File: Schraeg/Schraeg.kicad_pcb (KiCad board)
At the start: 2 copper layers, 84.5 x 128.5 mm, 116 parts, among them U1 TL074, U2 TL074, U3 V2164, U4 TL074, U5 TL074

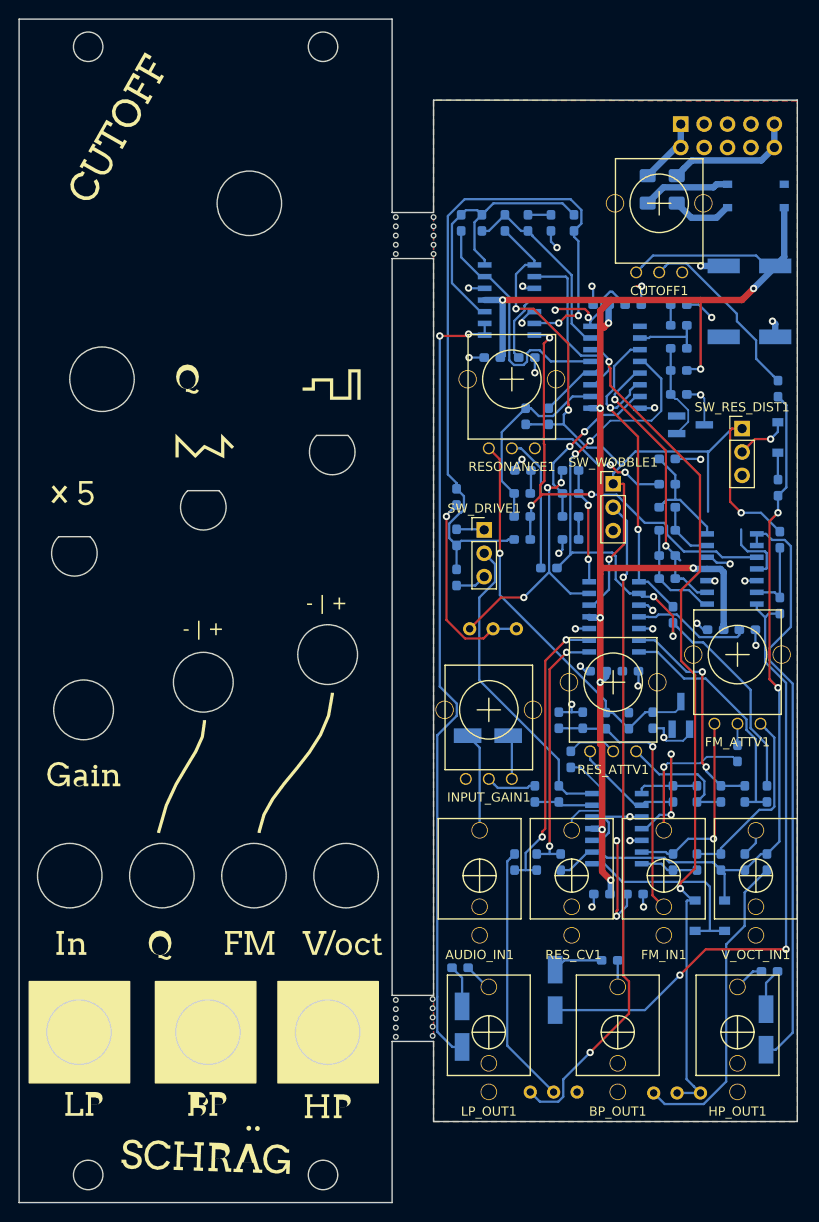
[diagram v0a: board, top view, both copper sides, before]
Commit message: Finished v0.2
* Flipped switches
* Enlarged switch holes
* Enlarged and enovaled pot support holes
* Reduced jack socket hole sizes
* Improved component and component reference locations

Archived v0.1 (previously know as the 2019 edition) and
re-exported schematics, gerbers, interactive BOM etc for
the 2021 Edition (v0.2).
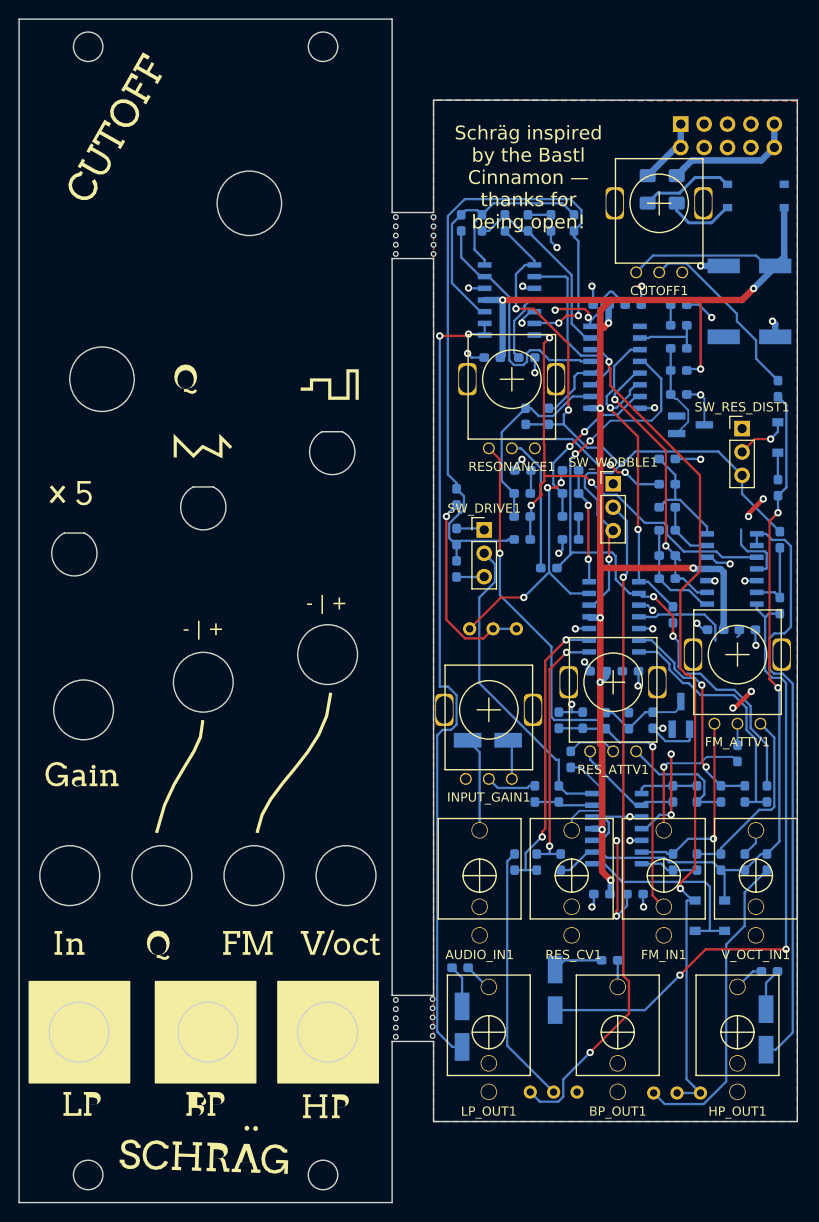
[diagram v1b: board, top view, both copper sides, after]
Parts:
- moved R22 4.45 mm to (47.5, 56.2), turned to 90 degrees
- moved R21 3.43 mm to (47.5, 59.7), turned to 270 degrees
- moved C2 0.50 mm to (50.9, 78.3)
- moved svg2mod 0.20 mm to (20.6, 64.5)
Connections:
- SW_DRIVE1 pad 1: Net-(R21-Pad2) -> Net-(R22-Pad2)
- SW_DRIVE1 pad 3: Net-(R22-Pad2) -> Net-(R21-Pad2)
- SW_RES_DIST1 pad 1: /Filter Core/RES_MOD -> (no net)
- SW_RES_DIST1 pad 3: (no net) -> /Filter Core/RES_MOD
- SW_WOBBLE1 pad 1: /Filter Core/RES_MOD -> (no net)
- SW_WOBBLE1 pad 3: (no net) -> /Filter Core/RES_MOD
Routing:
- net /Filter Core/RES_MOD: track 95.3 -> 83.3 mm, vias 4 -> 3
- net 5V_REF: track 44.7 -> 49.1 mm
- net +12V: track 61.8 -> 65.9 mm, vias 6 -> 10
- net Net-(C11-Pad2): track 23.8 -> 25.3 mm
- net /Filter Core/HP_OUT: track 64.0 -> 65.2 mm
- net GND: track 76.1 -> 77.3 mm
- net Net-(R13-Pad1): track 26.5 -> 27.6 mm
- net /Filter Core/LP_OUT: track 86.9 -> 87.9 mm
- net Net-(D5-Pad1): track 6.64 -> 7.57 mm
- net /Filter Core/AUDIO_IN: track 79.5 -> 78.7 mm
- net Net-(D5-Pad2): track 9.52 -> 10.1 mm
- net Net-(R28-Pad1): track 51.5 -> 52.1 mm
- net /Filter Core/BP_OUT: track 68.4 -> 68.9 mm
- net Net-(R11-Pad1): track 24.1 -> 23.6 mm
- net Net-(AUDIO_IN1-Pad3): track 10.8 -> 10.3 mm
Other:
- outline, holes or cut-outs redrawn
- board text added: "Schräg inspired by the Bastl Cinnamon — thanks for being open!"
- board text added: "Schräg v0.2 Barnaby Walters waterpigs.co.uk cc-by-sa 2021"
- board text removed: "Barnaby Walters waterpigs.co.uk cc-by-sa 2019"

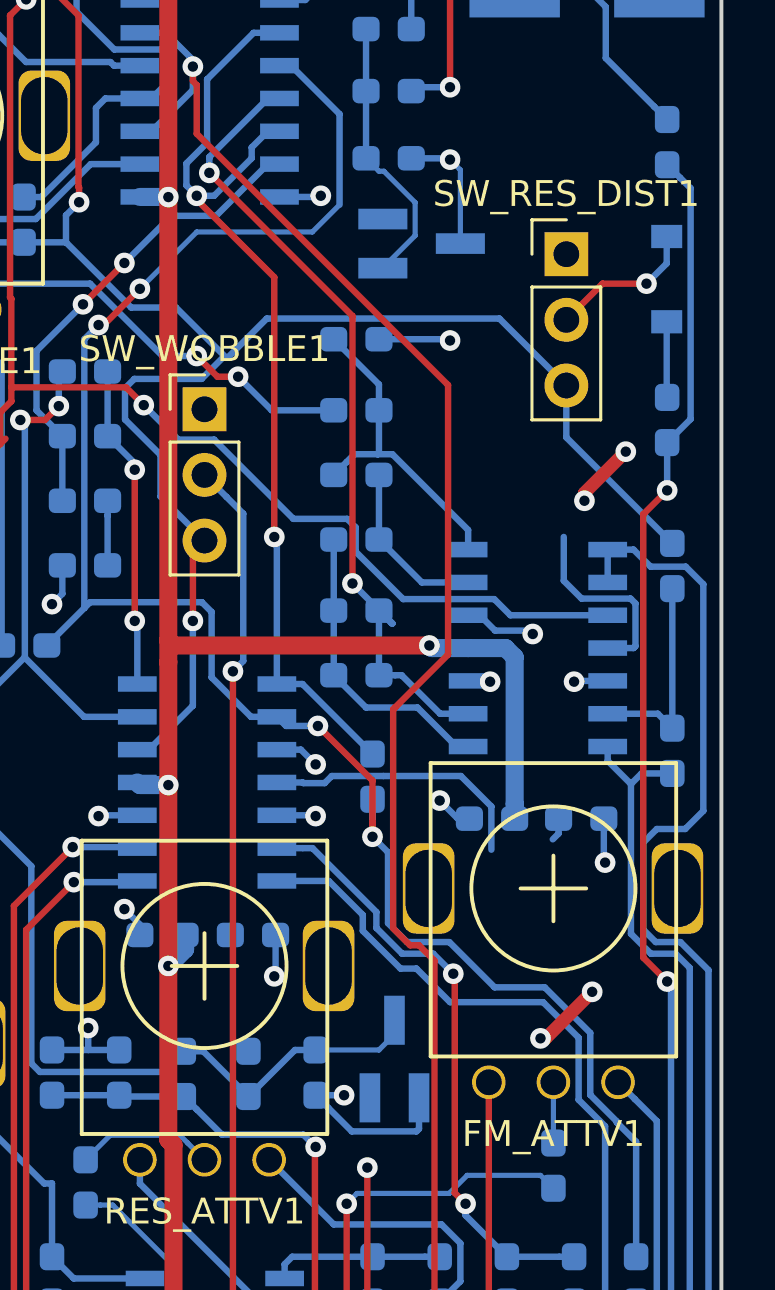
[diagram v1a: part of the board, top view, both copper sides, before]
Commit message: Fixed LM4040 symbols and PCB layout. Fixes #2
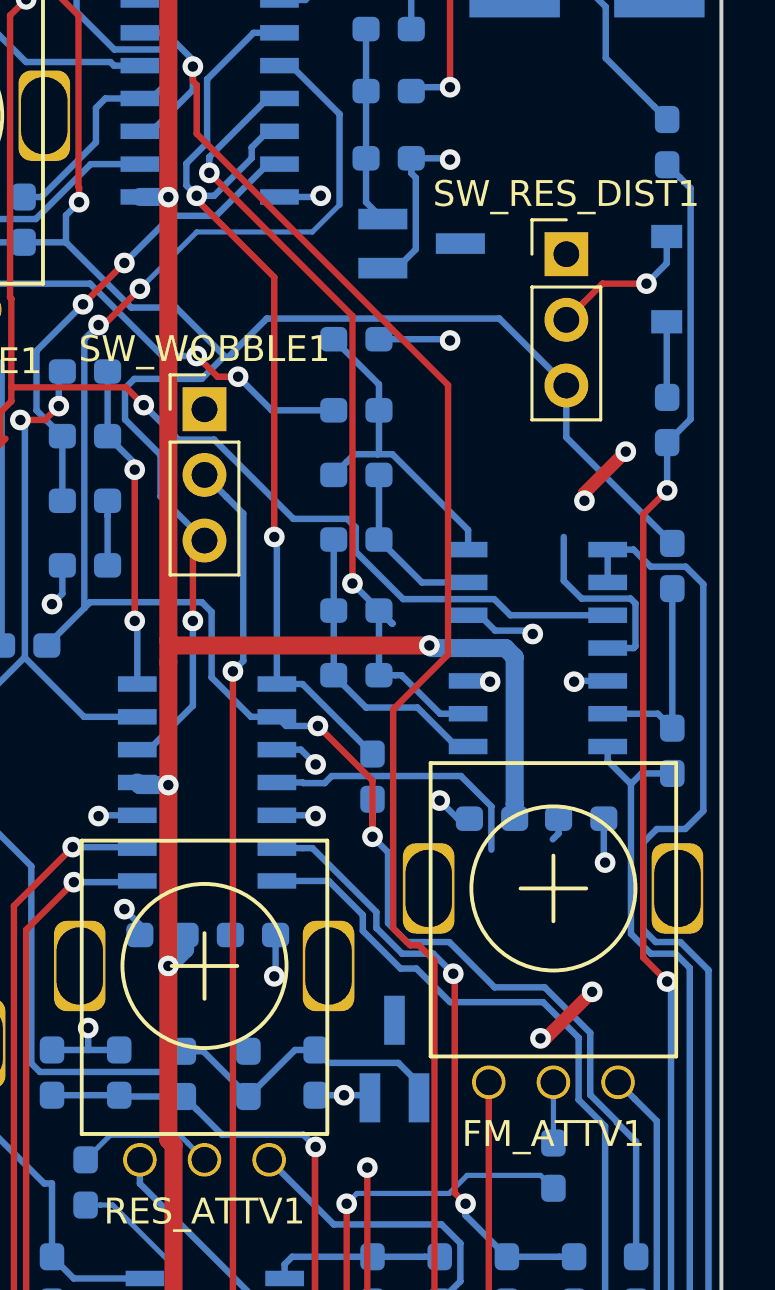
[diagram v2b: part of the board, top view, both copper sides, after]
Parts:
- D4, D6: value LM4040DCK-5 -> LM4040DBZ-5
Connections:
- D4 pad 1: GND -> 5V_REF
- D4 pad 2: (no net) -> GND
- D4 pad 3: 5V_REF -> (no net)
- D6 pad 1: -5V_REF -> GND
- D6 pad 2: (no net) -> -5V_REF
- D6 pad 3: GND -> (no net)
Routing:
- net -5V_REF: track 10.7 -> 7.62 mm
- net GND: track 77.3 -> 74.3 mm
- net 5V_REF: track 49.1 -> 50.4 mm
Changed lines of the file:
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@@
     (thickness 1.6)
     (drawings 233)
-    (tracks 934)
+    (tracks 932)
     (zones 0)
     (modules 116)
@@
       (effects (font (size 1 1) (thickness 0.15)) (justify mirror))
     )
-    (fp_text value LM4040DCK-5 (at 0 -2.5 90) (layer B.Fab)
+    (fp_text value LM4040DBZ-5 (at 0 -2.5 90) (layer B.Fab)
       (effects (font (size 1 1) (thickness 0.15)) (justify mirror))
     )
@@
       (effects (font (size 0.5 0.5) (thickness 0.075)) (justify mirror))
     )
-    (pad 3 smd rect (at 1.5 0 90) (size 1.9 0.8) (layers B.Cu B.Paste B.Mask)
-      (net 24 5V_REF))
-    (pad 2 smd rect (at -1.5 -0.95 90) (size 1.9 0.8) (layers B.Cu B.Paste B.Mask))
-    (pad 1 smd rect (at -1.5 0.95 90) (size 1.9 0.8) (layers B.Cu B.Paste B.Mask)
+    (pad 3 smd rect (at 1.5 0 90) (size 1.9 0.8) (layers B.Cu B.Paste B.Mask))
+    (pad 2 smd rect (at -1.5 -0.95 90) (size 1.9 0.8) (layers B.Cu B.Paste B.Mask)
       (net 1 GND))
+    (pad 1 smd rect (at -1.5 0.95 90) (size 1.9 0.8) (layers B.Cu B.Paste B.Mask)
+      (net 24 5V_REF))
     (model ${KISYS3DMOD}/Package_TO_SOT_SMD.3dshapes/SOT-23.wrl
       (at (xyz 0 0 0))
@@
       (effects (font (size 1 1) (thickness 0.15)) (justify mirror))
     )
-    (fp_text value LM4040DCK-5 (at 0 -2.5) (layer B.Fab)
+    (fp_text value LM4040DBZ-5 (at 0 -2.5) (layer B.Fab)
       (effects (font (size 1 1) (thickness 0.15)) (justify mirror))
     )
@@
     (fp_line (start 0.76 -1.58) (end -0.7 -1.58) (layer B.SilkS) (width 0.12))
     (pad 1 smd rect (at -1.5 0.95) (size 1.9 0.8) (layers B.Cu B.Paste B.Mask)
-      (net 28 -5V_REF))
-    (pad 2 smd rect (at -1.5 -0.95) (size 1.9 0.8) (layers B.Cu B.Paste B.Mask))
-    (pad 3 smd rect (at 1.5 0) (size 1.9 0.8) (layers B.Cu B.Paste B.Mask)
       (net 1 GND))
+    (pad 2 smd rect (at -1.5 -0.95) (size 1.9 0.8) (layers B.Cu B.Paste B.Mask)
+      (net 28 -5V_REF))
+    (pad 3 smd rect (at 1.5 0) (size 1.9 0.8) (layers B.Cu B.Paste B.Mask))
     (model ${KISYS3DMOD}/Package_TO_SOT_SMD.3dshapes/SOT-23.wrl
       (at (xyz 0 0 0))
@@
   (segment (start 67.4 42.245) (end 68.955 42.245) (width 0.25) (layer B.Cu) (net 1))
   (via (at 74 40.8) (size 0.8) (drill 0.4) (layers F.Cu B.Cu) (net 1))
-  (segment (start 73.95 40.75) (end 74 40.8) (width 0.25) (layer B.Cu) (net 1))
   (segment (start 72.5 40.75) (end 73.95 40.75) (width 0.25) (layer B.Cu) (net 1))
+  (segment (start 73.95 40.75) (end 74 40.8) (width 0.25) (layer B.Cu) (net 1))
   (via (at 74 47.8) (size 0.8) (drill 0.4) (layers F.Cu B.Cu) (net 1))
   (segment (start 73.95 47.75) (end 74 47.8) (width 0.25) (layer B.Cu) (net 1))
@@
   (segment (start 75.74499 59.02499) (end 77.06999 59.02499) (width 0.25) (layer B.Cu) (net 1))
   (segment (start 74.7 58.43) (end 75.15 58.43) (width 0.25) (layer B.Cu) (net 1))
-  (segment (start 74.399999 41.199999) (end 74 40.8) (width 0.2) (layer B.Cu) (net 1))
-  (segment (start 74.4 44.05) (end 74.399999 41.199999) (width 0.2) (layer B.Cu) (net 1))
   (segment (start 49.15 36.75) (end 48.7 36.3) (width 0.25) (layer B.Cu) (net 1))
   (via (at 48.7 36.3) (size 0.8) (drill 0.4) (layers F.Cu B.Cu) (net 1))
@@
   (segment (start 62 70.4) (end 61.4 69.8) (width 0.25) (layer B.Cu) (net 1))
   (segment (start 62 70.8) (end 62 70.4) (width 0.25) (layer B.Cu) (net 1))
-  (segment (start 69.299072 77.499072) (end 68.8 77) (width 0.25) (layer B.Cu) (net 1))
-  (segment (start 72.8 78.3) (end 72.7 78.4) (width 0.25) (layer B.Cu) (net 1))
-  (segment (start 70.2 78.4) (end 69.299072 77.499072) (width 0.25) (layer B.Cu) (net 1))
-  (segment (start 72.7 78.4) (end 70.2 78.4) (width 0.25) (layer B.Cu) (net 1))
-  (segment (start 72.8 77.1) (end 72.8 78.3) (width 0.25) (layer B.Cu) (net 1))
   (via (at 69.899998 77) (size 0.8) (drill 0.4) (layers F.Cu B.Cu) (net 1))
   (segment (start 68.8 77) (end 69.899998 77) (width 0.25) (layer B.Cu) (net 1))
@@
   (segment (start 64.45 75.3) (end 63.7 75.3) (width 0.25) (layer B.Cu) (net 24))
   (segment (start 66.2 77.05) (end 64.45 75.3) (width 0.25) (layer B.Cu) (net 24))
-  (segment (start 71.85 74.65) (end 71.85 74.1) (width 0.2) (layer B.Cu) (net 24))
-  (segment (start 71.25 75.25) (end 71.85 74.65) (width 0.2) (layer B.Cu) (net 24))
-  (segment (start 68.8 75.25) (end 71.25 75.25) (width 0.2) (layer B.Cu) (net 24))
   (segment (start 57.79999 68.138988) (end 57.79999 75.7705) (width 0.25) (layer B.Cu) (net 24))
   (segment (start 57.79999 75.7705) (end 58.12949 76.1) (width 0.25) (layer B.Cu) (net 24))
@@
   (segment (start 70.75 35.75) (end 70.75 38.15) (width 0.25) (layer B.Cu) (net 28))
   (segment (start 70.75 38.15) (end 70.75 40.75) (width 0.25) (layer B.Cu) (net 28))
-  (segment (start 71.249072 41.249072) (end 70.75 40.75) (width 0.2) (layer B.Cu) (net 28))
-  (segment (start 72.650001 42.459999) (end 71.439074 41.249072) (width 0.2) (layer B.Cu) (net 28))
-  (segment (start 71.439074 41.249072) (end 71.249072 41.249072) (width 0.2) (layer B.Cu) (net 28))
-  (segment (start 72.650001 43.740001) (end 72.650001 42.459999) (width 0.2) (layer B.Cu) (net 28))
-  (segment (start 71.390002 45) (end 72.650001 43.740001) (width 0.2) (layer B.Cu) (net 28))
-  (segment (start 71.4 45) (end 71.390002 45) (width 0.2) (layer B.Cu) (net 28))
+  (segment (start 71.4 45) (end 71.390002 45) (width 0.2) (layer B.Cu) (net 1))
+  (segment (start 70.8 77) (end 70.9 77.1) (width 0.25) (layer B.Cu) (net 1))
+  (segment (start 69.899998 77) (end 70.8 77) (width 0.25) (layer B.Cu) (net 1))
+  (segment (start 72.675001 44.274999) (end 71.95 45) (width 0.25) (layer B.Cu) (net 1))
+  (segment (start 72.675001 41.500001) (end 72.675001 44.274999) (width 0.25) (layer B.Cu) (net 1))
+  (segment (start 72.5 41.325) (end 72.675001 41.500001) (width 0.25) (layer B.Cu) (net 1))
+  (segment (start 71.95 45) (end 71.4 45) (width 0.25) (layer B.Cu) (net 1))
+  (segment (start 72.5 40.75) (end 72.5 41.325) (width 0.25) (layer B.Cu) (net 1))
+  (segment (start 72.8 76.55) (end 72.8 77.1) (width 0.25) (layer B.Cu) (net 24))
+  (segment (start 71.999072 75.749072) (end 72.8 76.55) (width 0.25) (layer B.Cu) (net 24))
+  (segment (start 69.299072 75.749072) (end 71.999072 75.749072) (width 0.25) (layer B.Cu) (net 24))
+  (segment (start 68.8 75.25) (end 69.299072 75.749072) (width 0.25) (layer B.Cu) (net 24))
+  (segment (start 70.75 42.45) (end 71.4 43.1) (width 0.25) (layer B.Cu) (net 28))
+  (segment (start 70.75 40.75) (end 70.75 42.45) (width 0.25) (layer B.Cu) (net 28))
   (segment (start 81.900928 38.750928) (end 82.4 39.25) (width 0.25) (layer B.Cu) (net 29))
   (segment (start 80.024999 34.889997) (end 80.024999 36.874999) (width 0.25) (layer B.Cu) (net 29))

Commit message: Updated board version reference
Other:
- board text added: "Schräg v0.2.1 Barnaby Walters waterpigs.co.uk cc-by-sa 2021"
- board text removed: "Schräg v0.2 Barnaby Walters waterpigs.co.uk cc-by-sa 2021"
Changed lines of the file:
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@@
   (gr_circle (center 20.5 110) (end 23.75 110) (layer Edge.Cuts) (width 0.15))
   (gr_circle (center 6.5 110) (end 9.75 110) (layer Edge.Cuts) (width 0.15))
-  (gr_text "Schräg v0.2\nBarnaby Walters\nwaterpigs.co.uk\ncc-by-sa 2021" (at 53.7 13.2) (layer B.SilkS)
+  (gr_text "Schräg v0.2.1\nBarnaby Walters\nwaterpigs.co.uk\ncc-by-sa 2021" (at 53.7 13.2) (layer B.SilkS)
     (effects (font (size 1 1) (thickness 0.25)) (justify mirror))
   )
@@
   (via (at 69.899998 77) (size 0.8) (drill 0.4) (layers F.Cu B.Cu) (net 1))
   (segment (start 68.8 77) (end 69.899998 77) (width 0.25) (layer B.Cu) (net 1))
+  (segment (start 71.4 45) (end 71.390002 45) (width 0.2) (layer B.Cu) (net 1))
+  (segment (start 70.8 77) (end 70.9 77.1) (width 0.25) (layer B.Cu) (net 1))
+  (segment (start 69.899998 77) (end 70.8 77) (width 0.25) (layer B.Cu) (net 1))
+  (segment (start 72.675001 44.274999) (end 71.95 45) (width 0.25) (layer B.Cu) (net 1))
+  (segment (start 72.675001 41.500001) (end 72.675001 44.274999) (width 0.25) (layer B.Cu) (net 1))
+  (segment (start 72.5 41.325) (end 72.675001 41.500001) (width 0.25) (layer B.Cu) (net 1))
+  (segment (start 71.95 45) (end 71.4 45) (width 0.25) (layer B.Cu) (net 1))
+  (segment (start 72.5 40.75) (end 72.5 41.325) (width 0.25) (layer B.Cu) (net 1))
   (segment (start 50 79.6) (end 48.7 78.3) (width 0.25) (layer B.Cu) (net 2))
   (segment (start 50 88.08) (end 50 79.6) (width 0.25) (layer B.Cu) (net 2))
@@
   (segment (start 62.9 76.1) (end 63.7 75.3) (width 0.25) (layer B.Cu) (net 24))
   (segment (start 58.12949 76.1) (end 62.9 76.1) (width 0.25) (layer B.Cu) (net 24))
+  (segment (start 72.8 76.55) (end 72.8 77.1) (width 0.25) (layer B.Cu) (net 24))
+  (segment (start 71.999072 75.749072) (end 72.8 76.55) (width 0.25) (layer B.Cu) (net 24))
+  (segment (start 69.299072 75.749072) (end 71.999072 75.749072) (width 0.25) (layer B.Cu) (net 24))
+  (segment (start 68.8 75.25) (end 69.299072 75.749072) (width 0.25) (layer B.Cu) (net 24))
   (segment (start 61.25 77.05) (end 61.2 77) (width 0.25) (layer B.Cu) (net 25))
   (segment (start 63.7 77.05) (end 61.25 77.05) (width 0.25) (layer B.Cu) (net 25))
@@
   (segment (start 70.75 35.75) (end 70.75 38.15) (width 0.25) (layer B.Cu) (net 28))
   (segment (start 70.75 38.15) (end 70.75 40.75) (width 0.25) (layer B.Cu) (net 28))
-  (segment (start 71.4 45) (end 71.390002 45) (width 0.2) (layer B.Cu) (net 1))
-  (segment (start 70.8 77) (end 70.9 77.1) (width 0.25) (layer B.Cu) (net 1))
-  (segment (start 69.899998 77) (end 70.8 77) (width 0.25) (layer B.Cu) (net 1))
-  (segment (start 72.675001 44.274999) (end 71.95 45) (width 0.25) (layer B.Cu) (net 1))
-  (segment (start 72.675001 41.500001) (end 72.675001 44.274999) (width 0.25) (layer B.Cu) (net 1))
-  (segment (start 72.5 41.325) (end 72.675001 41.500001) (width 0.25) (layer B.Cu) (net 1))
-  (segment (start 71.95 45) (end 71.4 45) (width 0.25) (layer B.Cu) (net 1))
-  (segment (start 72.5 40.75) (end 72.5 41.325) (width 0.25) (layer B.Cu) (net 1))
-  (segment (start 72.8 76.55) (end 72.8 77.1) (width 0.25) (layer B.Cu) (net 24))
-  (segment (start 71.999072 75.749072) (end 72.8 76.55) (width 0.25) (layer B.Cu) (net 24))
-  (segment (start 69.299072 75.749072) (end 71.999072 75.749072) (width 0.25) (layer B.Cu) (net 24))
-  (segment (start 68.8 75.25) (end 69.299072 75.749072) (width 0.25) (layer B.Cu) (net 24))
   (segment (start 70.75 42.45) (end 71.4 43.1) (width 0.25) (layer B.Cu) (net 28))
   (segment (start 70.75 40.75) (end 70.75 42.45) (width 0.25) (layer B.Cu) (net 28))
